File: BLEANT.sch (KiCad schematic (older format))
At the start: 29 parts, among them J1 Conn_01x04_Male, U1 nRF51x22-QFxx, X1 16MHz, X2 32.768kHz

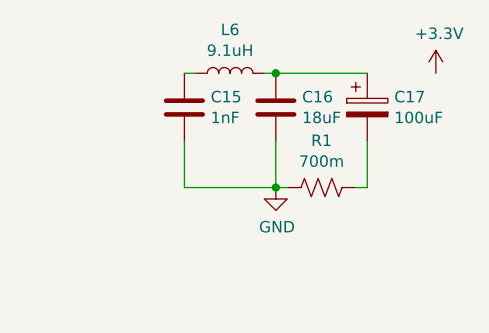
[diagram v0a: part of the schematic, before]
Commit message: Added footprints to most components; left out RF parts
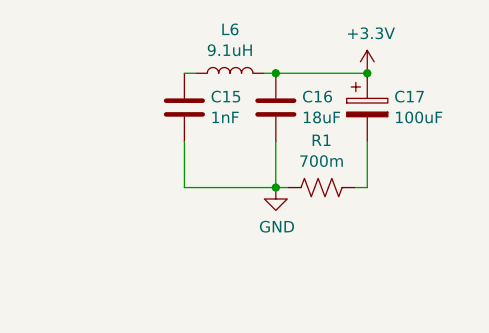
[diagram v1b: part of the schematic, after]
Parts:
- C1, C10, C11, C12, C13, C14, C15, C16, C2, C7, C8, C9: footprint (none) -> Capacitor_SMD:C_0805_2012Metric_Pad1.15x1.40mm_HandSolder
- J1: footprint (none) -> Connector_PinHeader_2.54mm:PinHeader_1x04_P2.54mm_Vertical
- L4, L5, L6: footprint (none) -> Inductor_SMD:L_0805_2012Metric_Pad1.15x1.40mm_HandSolder
- R1, R2: footprint (none) -> Resistor_SMD:R_0805_2012Metric_Pad1.15x1.40mm_HandSolder
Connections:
- net +3V3: now also C16.1, C17.1, L6.2
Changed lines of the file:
@@
 $EndDescr
 $Comp
-L power:+3.3V #PWR?
+L power:+3.3V #PWR0101
 U 1 1 5DF5598A
 P 3900 1150
-F 0 "#PWR?" H 3900 1000 50  0001 C CNN
+F 0 "#PWR0101" H 3900 1000 50  0001 C CNN
 F 1 "+3.3V" H 3915 1323 50  0000 C CNN
 F 2 "" H 3900 1150 50  0001 C CNN
@@
 F 0 "C7" V 3398 1150 50  0000 C CNN
 F 1 "4.7uF" V 3489 1150 50  0000 C CNN
-F 2 "" H 3688 1000 50  0001 C CNN
+F 2 "Capacitor_SMD:C_0805_2012Metric_Pad1.15x1.40mm_HandSolder" H 3688 1000 50  0001 C CNN
 F 3 "~" H 3650 1150 50  0001 C CNN
 	1    3650 1150
@@
 $EndComp
 $Comp
-L power:GND #PWR?
+L power:GND #PWR0102
 U 1 1 5DF5748A
 P 3900 6350
-F 0 "#PWR?" H 3900 6100 50  0001 C CNN
+F 0 "#PWR0102" H 3900 6100 50  0001 C CNN
 F 1 "GND" H 3905 6177 50  0000 C CNN
 F 2 "" H 3900 6350 50  0001 C CNN
@@
 F 0 "L4" H 4453 2646 50  0000 L CNN
 F 1 "10uH" H 4453 2555 50  0000 L CNN
-F 2 "" H 4400 2600 50  0001 C CNN
+F 2 "Inductor_SMD:L_0805_2012Metric_Pad1.15x1.40mm_HandSolder" H 4400 2600 50  0001 C CNN
 F 3 "~" H 4400 2600 50  0001 C CNN
 	1    4400 2600
@@
 F 0 "L5" H 4453 2346 50  0000 L CNN
 F 1 "15nH" H 4453 2255 50  0000 L CNN
-F 2 "" H 4400 2300 50  0001 C CNN
+F 2 "Inductor_SMD:L_0805_2012Metric_Pad1.15x1.40mm_HandSolder" H 4400 2300 50  0001 C CNN
 F 3 "~" H 4400 2300 50  0001 C CNN
 	1    4400 2300
@@
 F 0 "C12" V 4398 2150 50  0000 C CNN
 F 1 "1uF" V 4489 2150 50  0000 C CNN
-F 2 "" H 4688 2000 50  0001 C CNN
+F 2 "Capacitor_SMD:C_0805_2012Metric_Pad1.15x1.40mm_HandSolder" H 4688 2000 50  0001 C CNN
 F 3 "~" H 4650 2150 50  0001 C CNN
 	1    4650 2150
@@
 	4200 2150 4200 2750
 $Comp
-L power:GND #PWR?
+L power:GND #PWR0103
 U 1 1 5DF65AE3
 P 4800 2150
-F 0 "#PWR?" H 4800 1900 50  0001 C CNN
+F 0 "#PWR0103" H 4800 1900 50  0001 C CNN
 F 1 "GND" H 4805 1977 50  0000 C CNN
 F 2 "" H 4800 2150 50  0001 C CNN
@@
 Connection ~ 3500 1550
 $Comp
-L power:GND #PWR?
+L power:GND #PWR0104
 U 1 1 5DF67EF5
 P 3500 1550
-F 0 "#PWR?" H 3500 1300 50  0001 C CNN
+F 0 "#PWR0104" H 3500 1300 50  0001 C CNN
 F 1 "GND" H 3505 1377 50  0000 C CNN
 F 2 "" H 3500 1550 50  0001 C CNN
@@
 F 0 "C11" V 3398 1550 50  0000 C CNN
 F 1 "100nF" V 3489 1550 50  0000 C CNN
-F 2 "" H 3688 1400 50  0001 C CNN
+F 2 "Capacitor_SMD:C_0805_2012Metric_Pad1.15x1.40mm_HandSolder" H 3688 1400 50  0001 C CNN
 F 3 "~" H 3650 1550 50  0001 C CNN
 	1    3650 1550
@@
 F 0 "C8" V 3198 2600 50  0000 C CNN
 F 1 "100nF" V 3289 2600 50  0000 C CNN
-F 2 "" H 3488 2450 50  0001 C CNN
+F 2 "Capacitor_SMD:C_0805_2012Metric_Pad1.15x1.40mm_HandSolder" H 3488 2450 50  0001 C CNN
 F 3 "~" H 3450 2600 50  0001 C CNN
 	1    3450 2600
@@
 F 0 "C10" V 3198 2200 50  0000 C CNN
 F 1 "47nF" V 3289 2200 50  0000 C CNN
-F 2 "" H 3488 2050 50  0001 C CNN
+F 2 "Capacitor_SMD:C_0805_2012Metric_Pad1.15x1.40mm_HandSolder" H 3488 2050 50  0001 C CNN
 F 3 "~" H 3450 2200 50  0001 C CNN
 	1    3450 2200
@@
 	3900 1550 3900 2750
 $Comp
-L power:GND #PWR?
+L power:GND #PWR0105
 U 1 1 5DF744A6
 P 3300 2600
-F 0 "#PWR?" H 3300 2350 50  0001 C CNN
+F 0 "#PWR0105" H 3300 2350 50  0001 C CNN
 F 1 "GND" H 3305 2427 50  0000 C CNN
 F 2 "" H 3300 2600 50  0001 C CNN
@@
 F 0 "C9" V 4398 1750 50  0000 C CNN
 F 1 "1nF" V 4489 1750 50  0000 C CNN
-F 2 "" H 4688 1600 50  0001 C CNN
+F 2 "Capacitor_SMD:C_0805_2012Metric_Pad1.15x1.40mm_HandSolder" H 4688 1600 50  0001 C CNN
 F 3 "~" H 4650 1750 50  0001 C CNN
 	1    4650 1750
@@
 $EndComp
 $Comp
-L power:GND #PWR?
+L power:GND #PWR0106
 U 1 1 5DF80150
 P 2550 2550
-F 0 "#PWR?" H 2550 2300 50  0001 C CNN
+F 0 "#PWR0106" H 2550 2300 50  0001 C CNN
 F 1 "GND" H 2555 2377 50  0000 C CNN
 F 2 "" H 2550 2550 50  0001 C CNN
@@
 	2000 3950 1800 3950
 $Comp
-L power:GND #PWR?
+L power:GND #PWR0107
 U 1 1 5DF85D83
 P 1800 3950
-F 0 "#PWR?" H 1800 3700 50  0001 C CNN
+F 0 "#PWR0107" H 1800 3700 50  0001 C CNN
 F 1 "GND" H 1805 3777 50  0000 C CNN
 F 2 "" H 1800 3950 50  0001 C CNN
@@
 F 0 "C2" V 2048 4850 50  0000 C CNN
 F 1 "12pF" V 2139 4850 50  0000 C CNN
-F 2 "" H 2338 4700 50  0001 C CNN
+F 2 "Capacitor_SMD:C_0805_2012Metric_Pad1.15x1.40mm_HandSolder" H 2338 4700 50  0001 C CNN
 F 3 "~" H 2300 4850 50  0001 C CNN
 	1    2300 4850
@@
 F 0 "C1" V 2048 4250 50  0000 C CNN
 F 1 "12pF" V 2139 4250 50  0000 C CNN
-F 2 "" H 2338 4100 50  0001 C CNN
+F 2 "Capacitor_SMD:C_0805_2012Metric_Pad1.15x1.40mm_HandSolder" H 2338 4100 50  0001 C CNN
 F 3 "~" H 2300 4250 50  0001 C CNN
 	1    2300 4250
@@
 	2150 4250 2150 4850
 $Comp
-L power:GND #PWR?
+L power:GND #PWR0108
 U 1 1 5DF91313
 P 2150 4850
-F 0 "#PWR?" H 2150 4600 50  0001 C CNN
+F 0 "#PWR0108" H 2150 4600 50  0001 C CNN
 F 1 "GND" H 2155 4677 50  0000 C CNN
 F 2 "" H 2150 4850 50  0001 C CNN
@@
 F 0 "C14" V 998 4850 50  0000 C CNN
 F 1 "12pF" V 1089 4850 50  0000 C CNN
-F 2 "" H 1288 4700 50  0001 C CNN
+F 2 "Capacitor_SMD:C_0805_2012Metric_Pad1.15x1.40mm_HandSolder" H 1288 4700 50  0001 C CNN
 F 3 "~" H 1250 4850 50  0001 C CNN
 	1    1250 4850
@@
 F 0 "C13" V 998 4250 50  0000 C CNN
 F 1 "12pF" V 1089 4250 50  0000 C CNN
-F 2 "" H 1288 4100 50  0001 C CNN
+F 2 "Capacitor_SMD:C_0805_2012Metric_Pad1.15x1.40mm_HandSolder" H 1288 4100 50  0001 C CNN
 F 3 "~" H 1250 4250 50  0001 C CNN
 	1    1250 4250
@@
 	1100 4250 1100 4850
 $Comp
-L power:GND #PWR?
+L power:GND #PWR0109
 U 1 1 5DFAC69A
 P 1100 4850
-F 0 "#PWR?" H 1100 4600 50  0001 C CNN
+F 0 "#PWR0109" H 1100 4600 50  0001 C CNN
 F 1 "GND" H 1105 4677 50  0000 C CNN
 F 2 "" H 1100 4850 50  0001 C CNN
@@
 F 0 "J1" H 2308 5931 50  0000 C CNN
 F 1 "Conn_01x04_Male" H 2308 5840 50  0000 C CNN
-F 2 "" H 2200 5650 50  0001 C CNN
+F 2 "Connector_PinHeader_2.54mm:PinHeader_1x04_P2.54mm_Vertical" H 2200 5650 50  0001 C CNN
 F 3 "~" H 2200 5650 50  0001 C CNN
 	1    2200 5650
@@
 $EndComp
 $Comp
-L power:GND #PWR?
+L power:GND #PWR0110
 U 1 1 5DFB6ECA
 P 2400 5750
-F 0 "#PWR?" H 2400 5500 50  0001 C CNN
+F 0 "#PWR0110" H 2400 5500 50  0001 C CNN
 F 1 "GND" V 2405 5622 50  0000 R CNN
 F 2 "" H 2400 5750 50  0001 C CNN
@@
 $EndComp
 $Comp
-L power:+3.3V #PWR?
+L power:+3.3V #PWR0111
 U 1 1 5DFB7A76
 P 2400 5850
-F 0 "#PWR?" H 2400 5700 50  0001 C CNN
+F 0 "#PWR0111" H 2400 5700 50  0001 C CNN
 F 1 "+3.3V" V 2415 5978 50  0000 L CNN
 F 2 "" H 2400 5850 50  0001 C CNN
@@
 F 0 "C16" H 6665 1146 50  0000 L CNN
 F 1 "18uF" H 6665 1055 50  0000 L CNN
-F 2 "" H 6588 950 50  0001 C CNN
+F 2 "Capacitor_SMD:C_0805_2012Metric_Pad1.15x1.40mm_HandSolder" H 6588 950 50  0001 C CNN
 F 3 "~" H 6550 1100 50  0001 C CNN
 	1    6550 1100
@@
 F 0 "C15" H 6265 1146 50  0000 L CNN
 F 1 "1nF" H 6265 1055 50  0000 L CNN
-F 2 "" H 6188 950 50  0001 C CNN
+F 2 "Capacitor_SMD:C_0805_2012Metric_Pad1.15x1.40mm_HandSolder" H 6188 950 50  0001 C CNN
 F 3 "~" H 6150 1100 50  0001 C CNN
 	1    6150 1100
@@
 F 0 "L6" V 6540 950 50  0000 C CNN
 F 1 "9.1uH" V 6449 950 50  0000 C CNN
-F 2 "" H 6350 950 50  0001 C CNN
+F 2 "Inductor_SMD:L_0805_2012Metric_Pad1.15x1.40mm_HandSolder" H 6350 950 50  0001 C CNN
 F 3 "~" H 6350 950 50  0001 C CNN
 	1    6350 950
@@
 F 0 "R1" V 6955 1450 50  0000 C CNN
 F 1 "700m" V 6864 1450 50  0000 C CNN
-F 2 "" V 6790 1440 50  0001 C CNN
+F 2 "Resistor_SMD:R_0805_2012Metric_Pad1.15x1.40mm_HandSolder" V 6790 1440 50  0001 C CNN
 F 3 "~" H 6750 1450 50  0001 C CNN
 	1    6750 1450
@@
 Connection ~ 6550 1450
 $Comp
-L power:GND #PWR?
+L power:GND #PWR0112
 U 1 1 5DFC7314
 P 6550 1450
-F 0 "#PWR?" H 6550 1200 50  0001 C CNN
+F 0 "#PWR0112" H 6550 1200 50  0001 C CNN
 F 1 "GND" H 6555 1277 50  0000 C CNN
 F 2 "" H 6550 1450 50  0001 C CNN
@@
 $EndComp
 $Comp
-L power:+3.3V #PWR?
+L power:+3.3V #PWR0113
 U 1 1 5DFC7A19
-P 7250 950
-F 0 "#PWR?" H 7250 800 50  0001 C CNN
-F 1 "+3.3V" H 7265 1123 50  0000 C CNN
-F 2 "" H 7250 950 50  0001 C CNN
-F 3 "" H 7250 950 50  0001 C CNN
-	1    7250 950
+P 6950 950
+F 0 "#PWR0113" H 6950 800 50  0001 C CNN
+F 1 "+3.3V" H 6965 1123 50  0000 C CNN
+F 2 "" H 6950 950 50  0001 C CNN
+F 3 "" H 6950 950 50  0001 C CNN
+	1    6950 950
 	1    0    0    -1
 $EndComp
@@
 F 0 "R2" H 2868 5446 50  0000 L CNN
 F 1 "10k" H 2868 5355 50  0000 L CNN
-F 2 "" V 2840 5390 50  0001 C CNN
+F 2 "Resistor_SMD:R_0805_2012Metric_Pad1.15x1.40mm_HandSolder" V 2840 5390 50  0001 C CNN
 F 3 "~" H 2800 5400 50  0001 C CNN
 	1    2800 5400
@@
 $EndComp
 $Comp
-L power:+3.3V #PWR?
+L power:+3.3V #PWR0114
 U 1 1 5DFC9566
 P 2800 5250
-F 0 "#PWR?" H 2800 5100 50  0001 C CNN
+F 0 "#PWR0114" H 2800 5100 50  0001 C CNN
 F 1 "+3.3V" H 2815 5423 50  0000 C CNN
 F 2 "" H 2800 5250 50  0001 C CNN
@@
 Wire Wire Line
 	2400 5650 3000 5650
+Connection ~ 6950 950
 $EndSCHEMATC

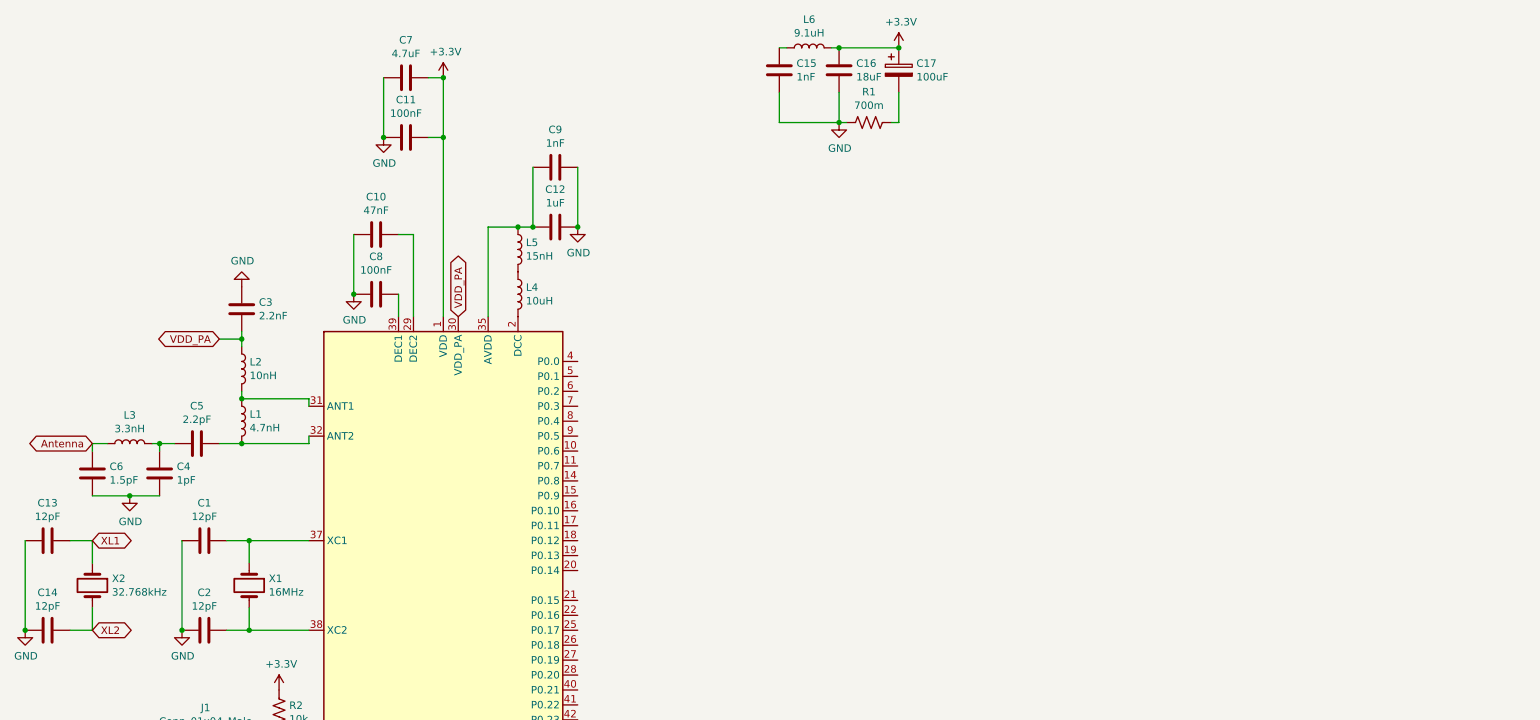
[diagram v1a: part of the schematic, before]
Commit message: Added stack template, temperature sensor, and crystal oscillator
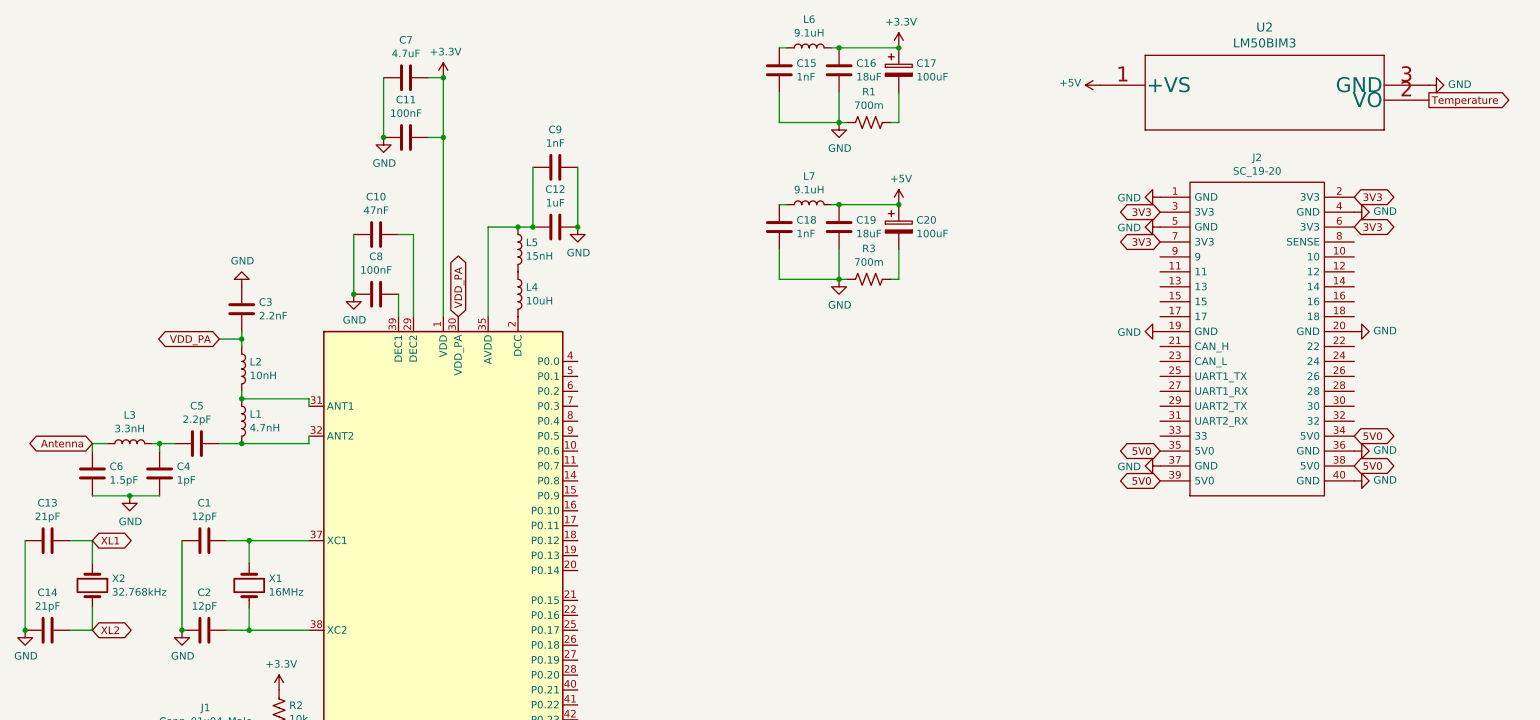
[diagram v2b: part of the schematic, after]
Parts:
- added C18: 1nF, Capacitor_SMD:C_0805_2012Metric_Pad1.15x1.40mm_HandSolder, symbol Device:C
- added C19: 18uF, Capacitor_SMD:C_0805_2012Metric_Pad1.15x1.40mm_HandSolder, symbol Device:C
- added C20: 100uF, symbol Device:CP
- added J2: SC_19-20, MASA_Library:Stack_Connector_2019_2020, symbol MASA_Library:SC_19-20
- added L7: 9.1uH, Inductor_SMD:L_0805_2012Metric_Pad1.15x1.40mm_HandSolder, symbol Device:L
- added R3: 700m, Resistor_SMD:R_0805_2012Metric_Pad1.15x1.40mm_HandSolder, symbol Device:R_US
- added U2: LM50BIM3, footprints:LM50_DBZ_3, symbol 2019-12-19_22-46-35:LM50BIM3
- C13, C14: value 12pF -> 21pF
- X1: footprint (none) -> Crystal:Crystal_SMD_2520-4Pin_2.5x2.0mm
- X2: footprint (none) -> Crystal:Crystal_SMD_MicroCrystal_CC7V-T1A-2Pin_3.2x1.5mm
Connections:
- net GND: now also C18.2, C19.2, J2.1 (GND), J2.19 (GND), J2.20 (GND), J2.36 (GND), J2.37 (GND), J2.4 (GND), J2.40 (GND), J2.5 (GND), R3.1, U2.3 (GND)
- new net: C18.1, L7.1
- new net: C20.2, R3.2
- new net +5V: C19.1, C20.1, L7.2, U2.1 (+VS)
- new net 3V3: J2.2 (3V3), J2.3 (3V3), J2.6 (3V3), J2.7 (3V3)
- new net 5V0: J2.34 (5V0), J2.35 (5V0), J2.38 (5V0), J2.39 (5V0)
- new net Temperature: U2.2 (VO)

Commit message: I did way too much for one commit
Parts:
- removed X1: 16MHz, Crystal:Crystal_SMD_2520-4Pin_2.5x2.0mm, symbol Device:Crystal
- added C21: 0.54uF, symbol Device:C
- added C22: 0.9uF, symbol Device:C
- added IC1, IC2: FAN4010IL6X_F113, FAN4010:6-LEAD_MICROPAK, symbol FAN4010IL6X_F113:FAN4010IL6X_F113
- added J3, J4: Conn_01x02, Connector_PinHeader_2.54mm:PinHeader_1x02_P2.54mm_Vertical, symbol Connector_Generic:Conn_01x02
- added R4, R5: 820k, Resistor_SMD:R_0805_2012Metric_Pad1.15x1.40mm_HandSolder, symbol Device:R_US
- added R6: 1, Resistor_SMD:R_0805_2012Metric_Pad1.15x1.40mm_HandSolder, symbol Device:R_US
- added R7, R9: R, Resistor_SMD:R_0805_2012Metric_Pad1.15x1.40mm_HandSolder, symbol Device:R_US
- added R8: 3k, Resistor_SMD:R_0805_2012Metric_Pad1.15x1.40mm_HandSolder, symbol Device:R_US
- added U3, U4: MP5077GG-Z, MASA_Library:MP5077GG-Z, symbol MASA_Library:MP5077GG-Z
- added Y1: 16MHz, Crystal:Crystal_SMD_2520-4Pin_2.5x2.0mm, symbol Device:Crystal_GND24
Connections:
- net +3V3: now also IC1.6 (LOAD), IC2.6 (LOAD), R6.1; no longer C16.1, C17.1, L6.2
- net +5V: now also R7.1; no longer C19.1, C20.1, L7.2
- net 3V3: now also J4.2 (Pin_2), U3.11 (Vin), U3.6 (Vin)
- net 5V0: now also J3.2 (Pin_2), U3.1 (EN), U3.3 (Vcc), U4.1 (EN), U4.11 (Vin), U4.3 (Vcc), U4.6 (Vin)
- net GND: now also C21.1, C22.1, IC1.5 (GND), IC2.5 (GND), R4.1, R5.1, R8.2, R9.2, U3.2 (GND), U4.2 (GND), Y1.2, Y1.4
- net at C1.1, U1.37 (XC1): now also Y1.1
- net at C2.1, U1.38 (XC2): now also Y1.3
- net at C15.1, L6.1: now also J4.1 (Pin_1), U3.10 (Vout), U3.7 (Vout), U3.8 (Vout), U3.9 (Vout)
- net at C18.1, L7.1: now also J3.1 (Pin_1), U4.10 (Vout), U4.7 (Vout), U4.8 (Vout), U4.9 (Vout)
- new net: C16.1, C17.1, IC1.1 (VIN), L6.2, R6.2
- new net: C19.1, C20.1, IC2.1 (VIN), L7.2, R7.2
- new net: R4.2, U3.4 (Ilim)
- new net: C21.2, U3.5 (SS)
- new net: R5.2, U4.4 (Ilim)
- new net: C22.2, U4.5 (SS)
- new net 3V3Sense: IC1.3 (IOUT), R8.1
- new net 5V0Sense: IC2.3 (IOUT), R9.1
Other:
- moved on the sheet: C15, C16, C17, C18, C19, C20, J2, L6, L7, R1, R3, U2
